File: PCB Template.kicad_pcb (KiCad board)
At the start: 2 copper layers, 76.2 x 76.2 mm, 0 parts

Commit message: Added stack board connector
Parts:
- added J1: SC_19-20, MASA_Library:Stack_Connector_2019_2020, F.Cu at (152.4, 127.0)

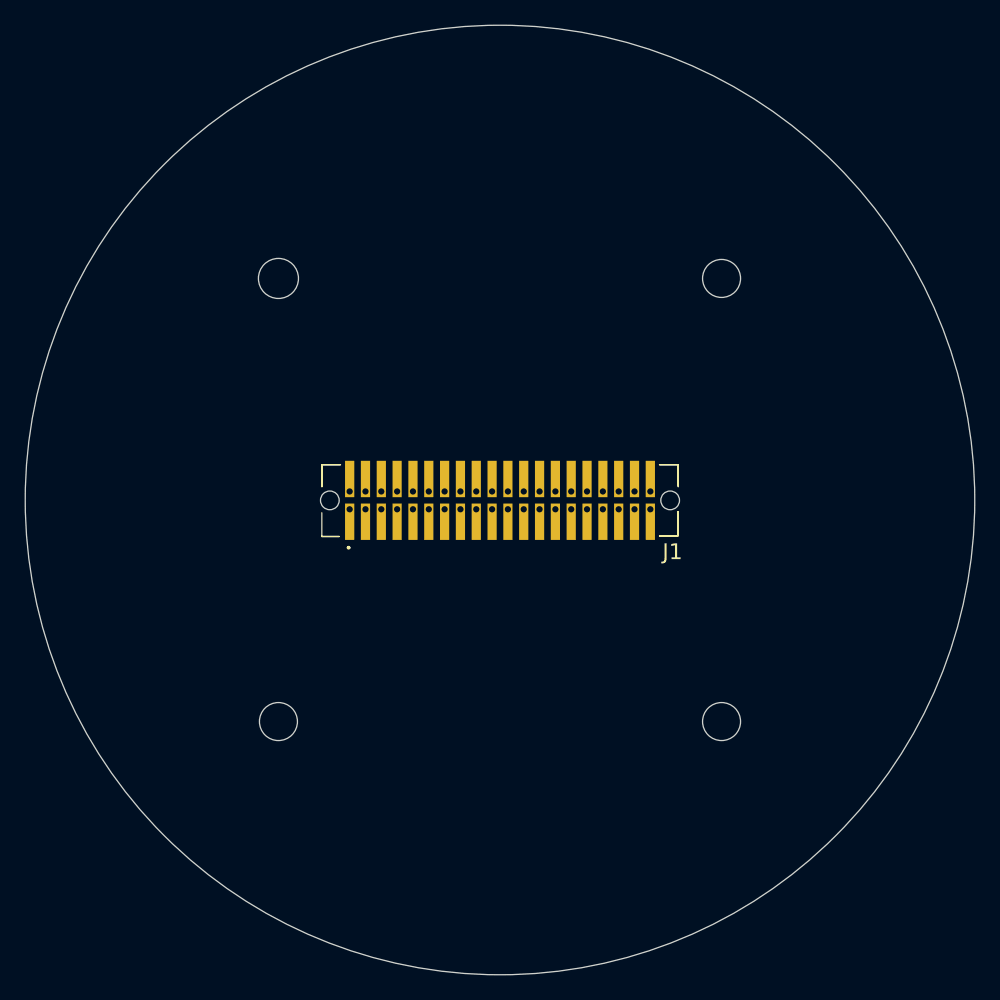
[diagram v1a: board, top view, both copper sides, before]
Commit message: Added routing slot
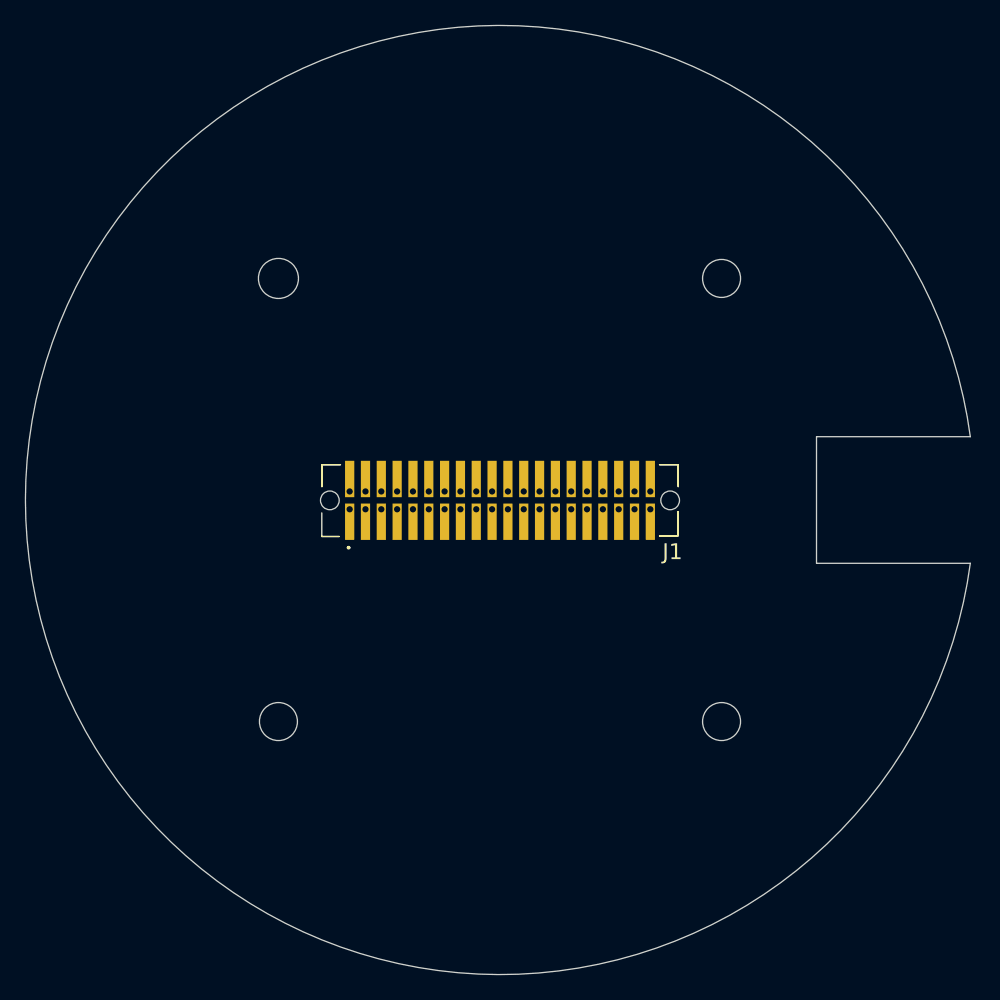
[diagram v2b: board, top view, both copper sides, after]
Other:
- board size 76.2 x 76.2 mm -> 75.8 x 76.2 mm
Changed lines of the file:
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@@
   (general
     (thickness 1.6)
-    (drawings 15)
+    (drawings 18)
     (tracks 0)
     (zones 0)
@@
     )
   )
+  (gr_arc (start 152.4 127) (end 190.1444 121.92) (angle -344.6693046) (layer Edge.Cuts) (width 0.05))
+  (gr_line (start 177.8 132.08) (end 190.1444 132.08) (layer Edge.Cuts) (width 0.05))
+  (gr_line (start 177.8 121.92) (end 177.8 132.08) (layer Edge.Cuts) (width 0.05))
+  (gr_line (start 190.1444 121.92) (end 177.8 121.92) (layer Edge.Cuts) (width 0.05))
   (dimension 76.2 (width 0.15) (layer Dwgs.User)
     (gr_text "3.0000 in" (at 152.4 171.48) (layer Dwgs.User)
@@
   (gr_circle (center 152.4 127) (end 152.4 101.6) (layer Dwgs.User) (width 0.15))
   (gr_circle (center 152.4 127) (end 149.86 127) (layer Dwgs.User) (width 0.15))
-  (gr_circle (center 152.4 127) (end 152.4 165.1) (layer Edge.Cuts) (width 0.05))
 )
